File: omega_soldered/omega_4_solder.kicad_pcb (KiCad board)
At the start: 2 copper layers, 204.8 x 76.2 mm, 77 parts, among them U1 ProMicro

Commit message: generate production files
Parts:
- removed H1, H2, H3, H4: Hole, MountingHole:MountingHole_2.2mm_M2
- added MX37: MX-NoLED, MX_Only:MXOnly-6U-Centered-ReversedStabilizers-NoLED, F.Cu at (167.8, 122.7)
- moved D33 10.7 mm to (176.1, 124.9)
- moved JP1 4.83 mm to (56.7, 55.4)
- moved D1 0.88 mm to (66.2, 65.7)
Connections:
- U1 pad 10: COL7 -> ROW2
- U1 pad 11: COL6 -> ROW3
- U1 pad 12: COL5 -> COL2
- U1 pad 13: COL4 -> COL5
- U1 pad 14: COL3 -> COL6
- U1 pad 15: COL2 -> COL7
- U1 pad 16: COL1 -> COL8
- U1 pad 17: ROW0 -> COL9
- U1 pad 18: ROW1 -> COL4
- U1 pad 19: ROW2 -> COL3
- U1 pad 20: COL0 -> COL1
- U1 pad 7: Net-(U1-Pad7) -> COL0
- U1 pad 8: COL9 -> ROW0
- U1 pad 9: COL8 -> ROW1
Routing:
- net COL9: track 75.0 -> 236.2 mm
- net COL8: track 74.0 -> 213.3 mm
- net COL7: track 49.4 -> 166.9 mm
- net COL6: track 49.8 -> 145.8 mm
- net COL5: track 90.7 -> 170.4 mm
- net COL4: track 49.2 -> 116.9 mm
- net ROW3: track 175.3 -> 237.4 mm
- net COL3: track 48.9 -> 99.4 mm
- net ROW2: track 171.4 -> 212.0 mm
- net COL1: track 49.5 -> 87.9 mm
- net COL0: track 49.7 -> 84.0 mm
- net COL2: track 49.6 -> 72.9 mm
- net Net-(D33-Pad2): track 21.6 -> 42.1 mm
- net ROW1: track 171.4 -> 190.7 mm
- net ROW0: track 171.3 -> 179.8 mm
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- added copper zone on B.Cu, net GND
- added copper zone on F.Cu, net GND
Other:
- board size 204.8 x 76.2 mm -> 204.8 x 78 mm
- board text added: "6u-centered"
- board text added: "8u 10u 6u-offcenter"
- board text added: "omega4_v0 by makenova"

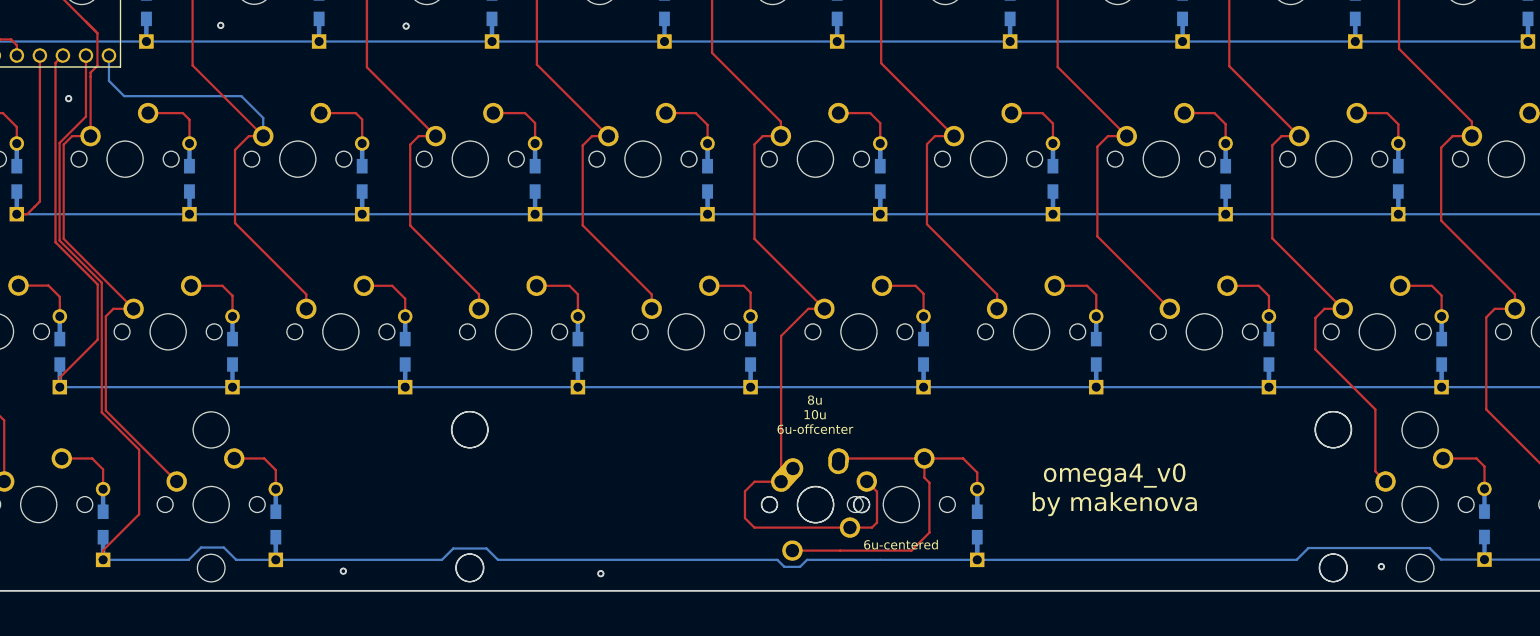
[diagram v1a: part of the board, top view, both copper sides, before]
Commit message: update spacebars on omega4
fix spacebar positioning on omega4
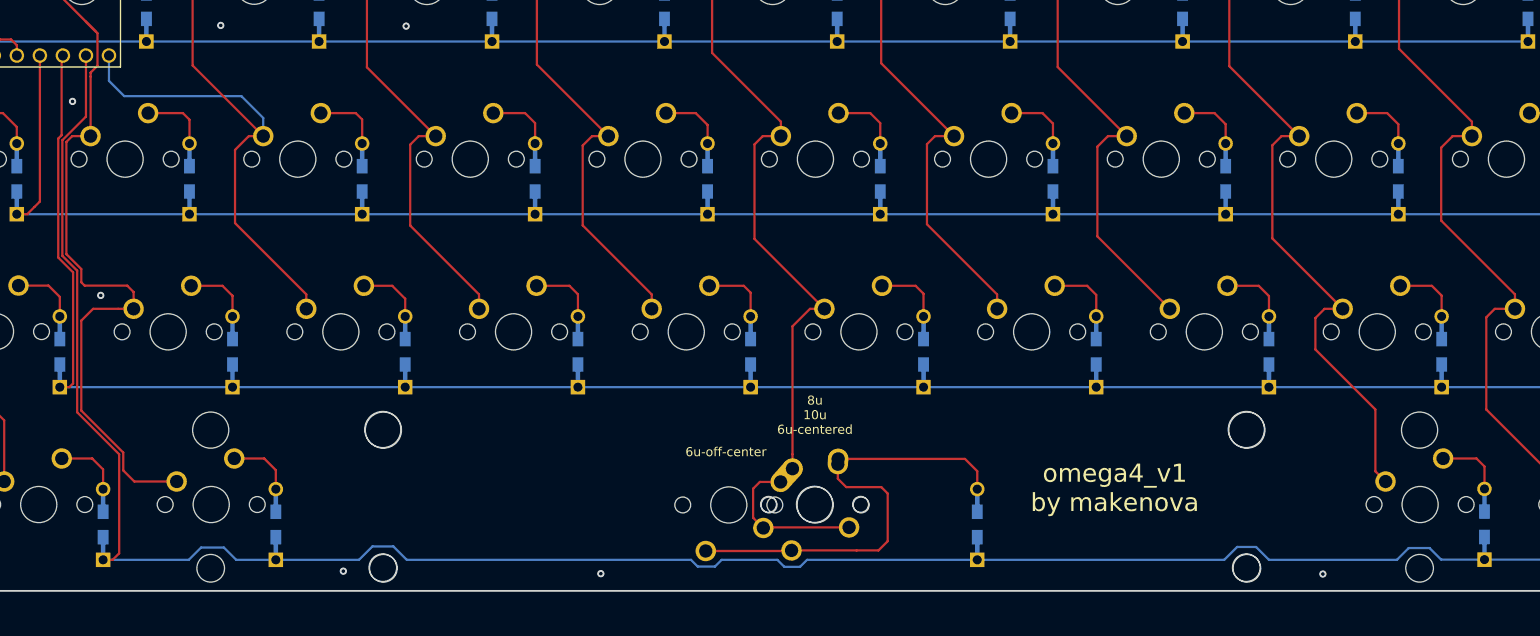
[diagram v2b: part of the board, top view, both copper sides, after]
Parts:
- MX37: footprint MX_Only:MXOnly-6U-Centered-ReversedStabilizers-NoLED -> MX_Only:MXOnly-6U-Centered-NoLED
- moved MX37 9.57 mm to (158.2, 122.7), turned to 180 degrees
- moved MX36 9.56 mm to (158.2, 122.7)
- moved MX33 0.06 mm to (158.2, 122.7)
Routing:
- net COL5: track 170.4 -> 158.3 mm
- net Net-(D33-Pad2): track 42.1 -> 51.4 mm
- net COL1: track 87.9 -> 96.7 mm
- net ROW2: track 212.0 -> 210.1 mm
- net ROW3: track 237.4 -> 237.9 mm
- net GND: vias 10 -> 11
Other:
- board text added: "6u-off-center"
- board text added: "8u 10u 6u-centered"
- board text added: "omega4_v1 by makenova"
- board text removed: "6u-centered"
- board text removed: "8u 10u 6u-offcenter"
- board text removed: "omega4_v0 by makenova"

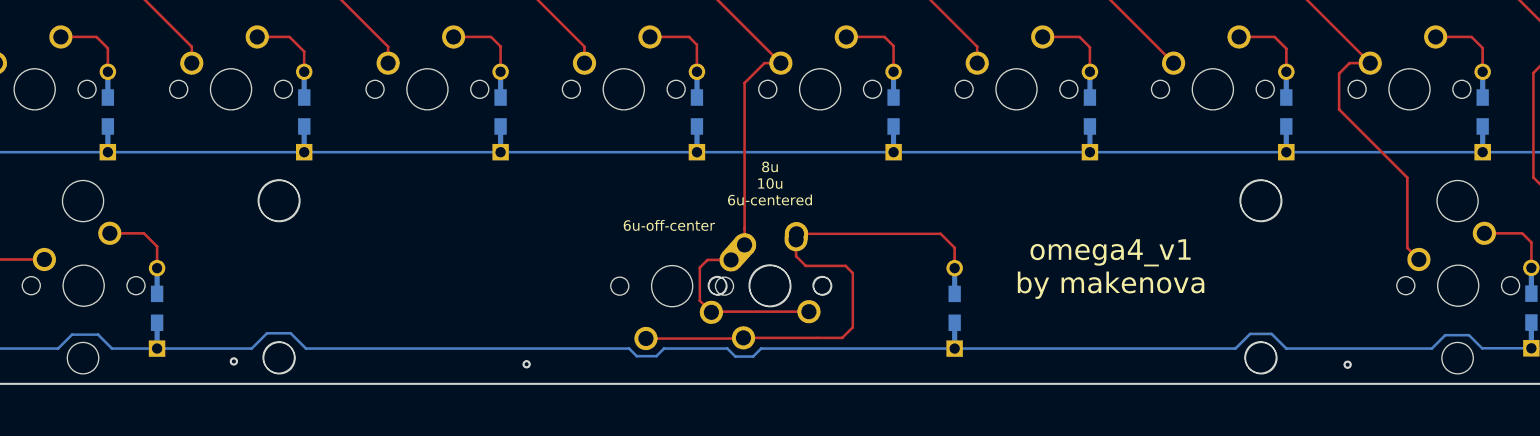
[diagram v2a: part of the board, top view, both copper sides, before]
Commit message: update omega4 case files
move stabilizer cutouts
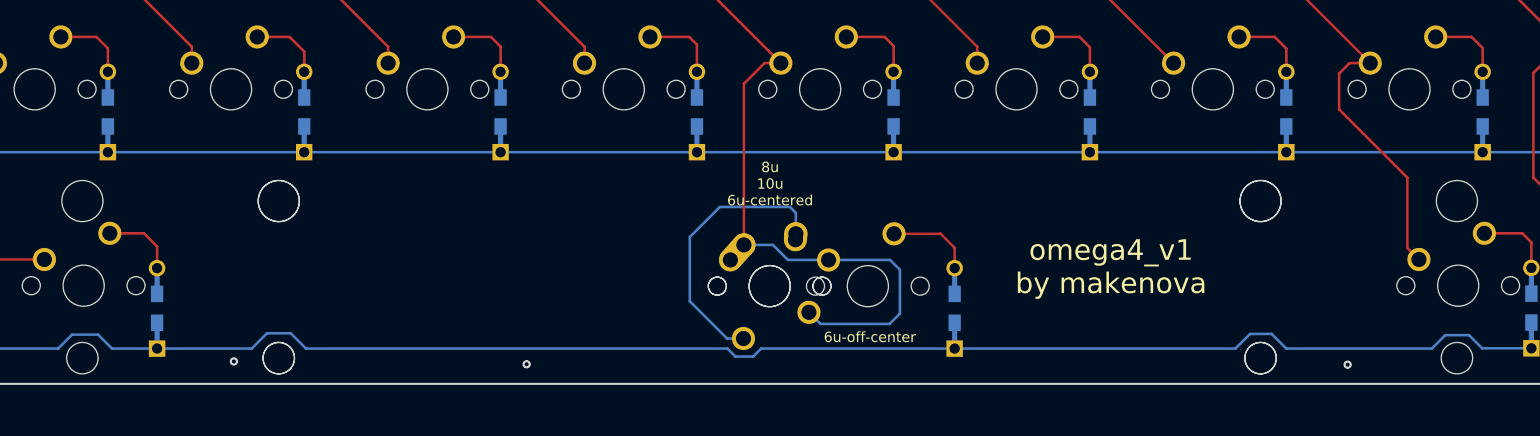
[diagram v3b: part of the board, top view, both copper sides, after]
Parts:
- MX36: footprint MX_Only:MXOnly-6U-NoLED -> MX_Only:MXOnly-6U-ReversedStabilizers-NoLED
- moved MX37 0.06 mm to (158.2, 122.7)
- moved MX33 0.06 mm to (158.2, 122.7)
- moved MX36 0.06 mm to (158.2, 122.7), turned to 0 degrees
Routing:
- net Net-(D33-Pad2): track 51.4 -> 35.2 mm
- net COL5: track 158.3 -> 170.8 mm
- net ROW3: track 237.9 -> 237.3 mm

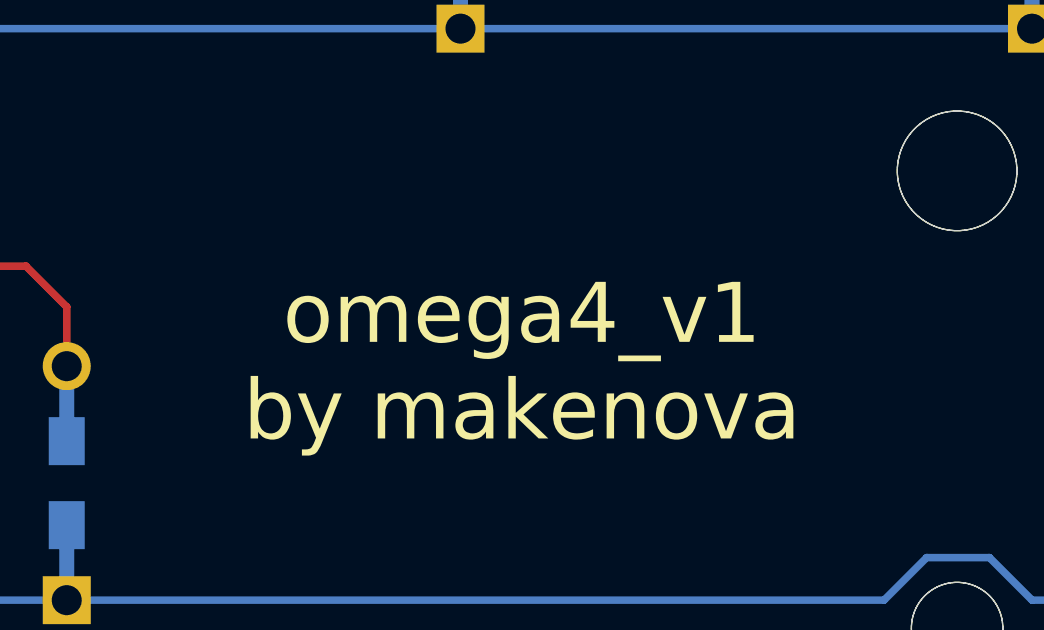
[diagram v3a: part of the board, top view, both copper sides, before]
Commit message: update soldered omega
increase stanoff hole size through the pcb
update stl files and step files
shuffle file locations
regenerate gerbers
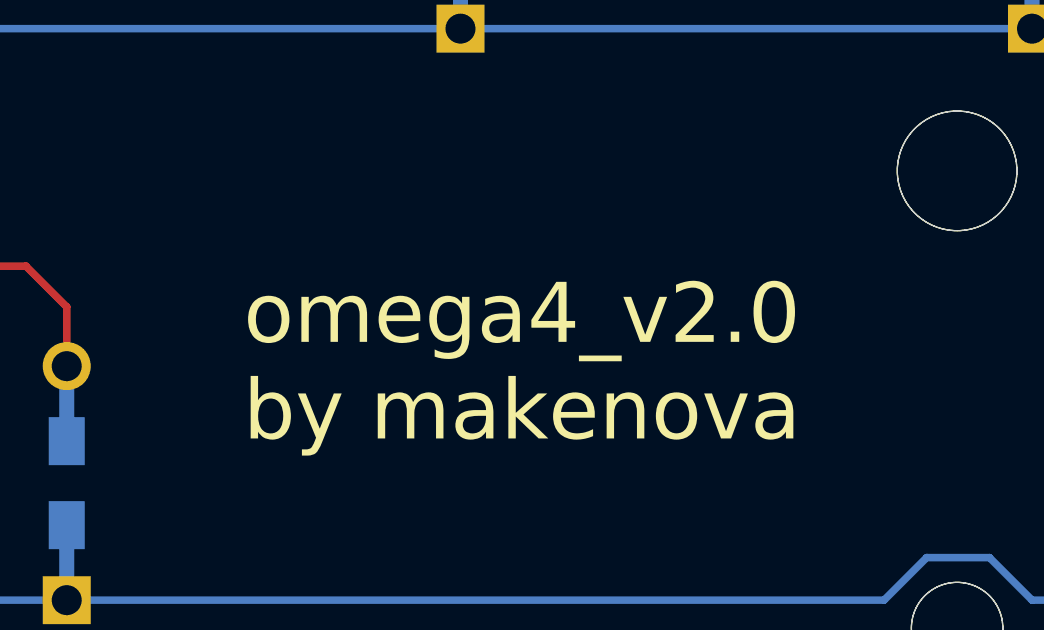
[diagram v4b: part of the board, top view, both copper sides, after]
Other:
- board text added: "omega4_v2.0 by makenova"
- board text removed: "omega4_v1 by makenova"
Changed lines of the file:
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@@
     (effects (font (size 1 1) (thickness 0.15)))
   )
-  (gr_text "omega4_v1\nby makenova" (at 191.3 120.875) (layer F.SilkS)
+  (gr_text "omega4_v2.0\nby makenova" (at 191.3 120.875) (layer F.SilkS)
     (effects (font (size 2 2) (thickness 0.2)))
   )

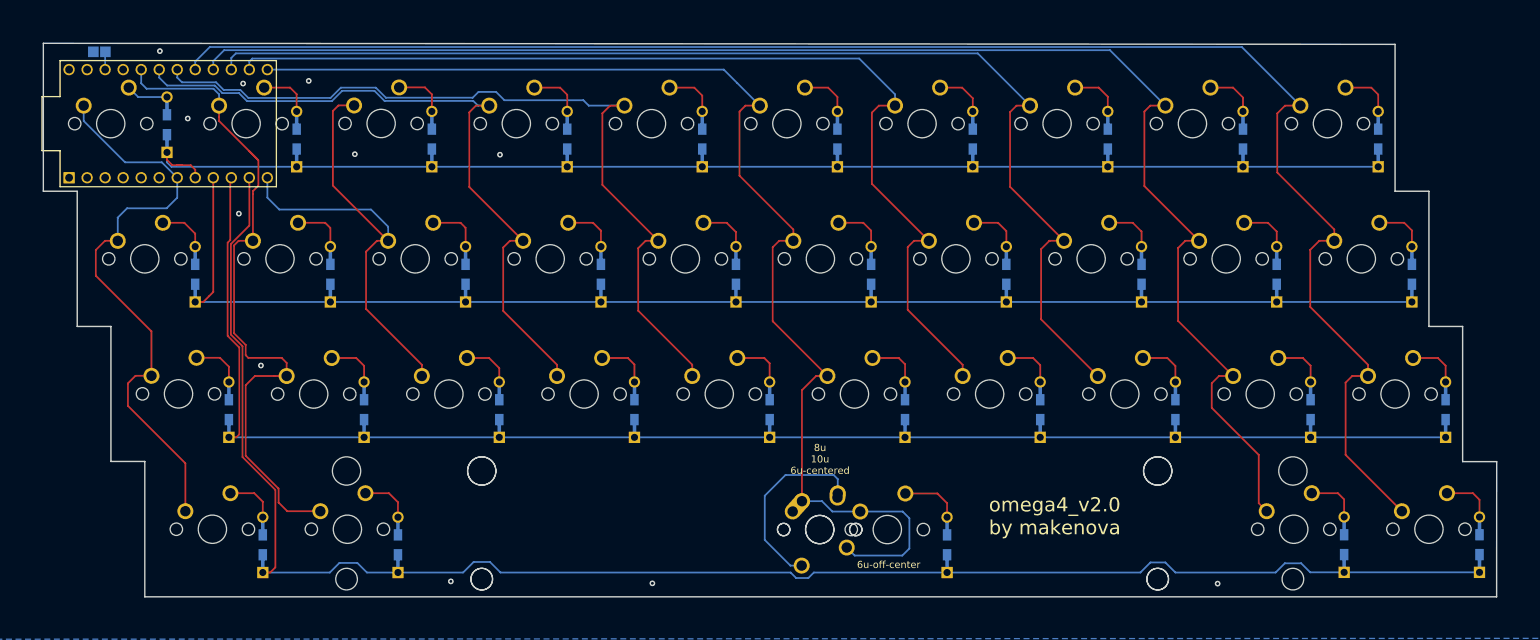
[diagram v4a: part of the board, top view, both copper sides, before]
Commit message: wip: v3
break away bottom row
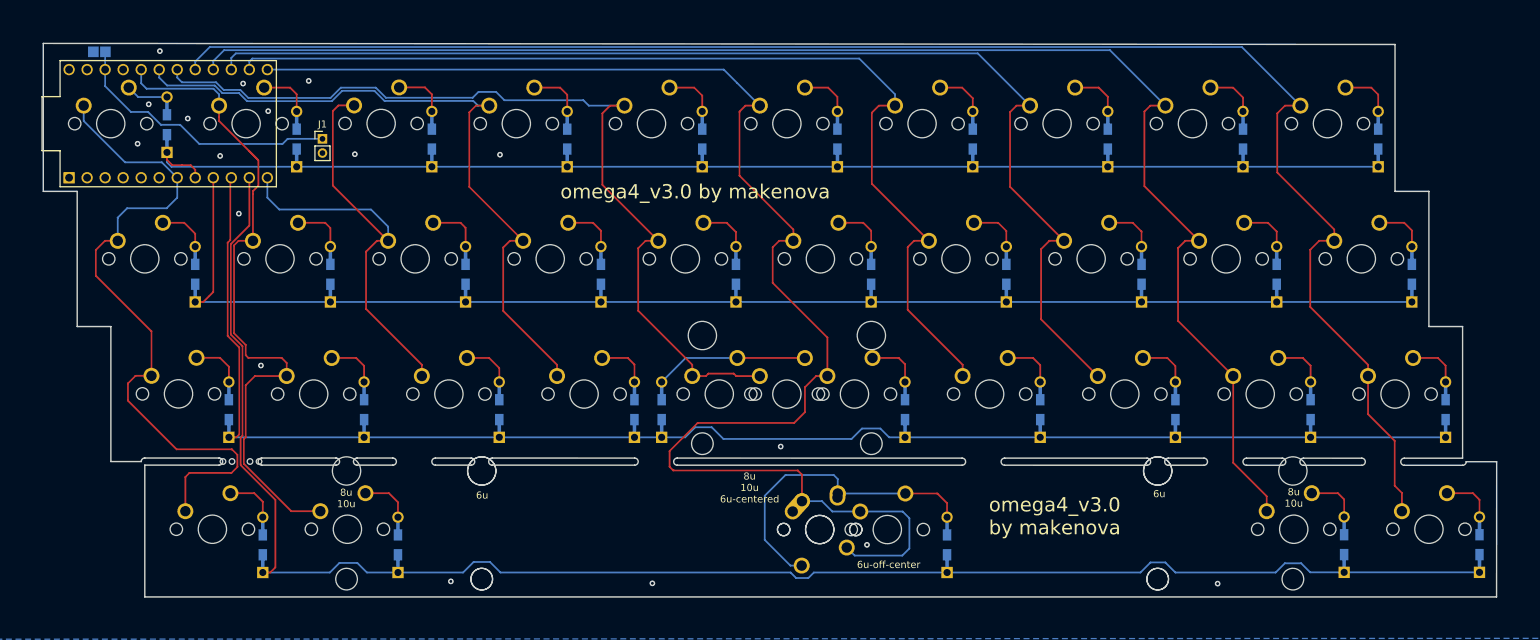
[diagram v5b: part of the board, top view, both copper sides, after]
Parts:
- added G***: LOGO, LOGO, B.Cu at (154.0, 81.3)
- added J1: Conn_01x02_Female, Connector_PinHeader_2.00mm:PinHeader_1x02_P2.00mm_Vertical, F.Cu at (88.1, 67.7)
- added MX38: MX-NoLED, MX_Only:MXOnly-2U-ReversedStabilizers-NoLED, F.Cu at (153.6, 103.7)
- added REF**: breakaway-mousebites, Keebio-Parts:breakaway-mousebites, F.Cu at (76.6, 113.4)
- moved D25 15.2 mm to (135.9, 105.8)
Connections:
- net Net-(JP1-Pad1) renamed RST
- U1 pad 1: Net-(U1-Pad1) -> unconnected-(U1-Pad1)
- U1 pad 2: Net-(U1-Pad2) -> unconnected-(U1-Pad2)
- U1 pad 24: Net-(U1-Pad24) -> unconnected-(U1-Pad24)
- U1 pad 5: Net-(U1-Pad5) -> unconnected-(U1-Pad5)
- U1 pad 6: Net-(U1-Pad6) -> unconnected-(U1-Pad6)
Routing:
- net RST: track 2.52 -> 39.2 mm
- net COL5: track 170.8 -> 204.5 mm
- net COL0: track 84.0 -> 98.1 mm
- net Net-(D25-Pad2): track 7.50 -> 21.6 mm
- net COL4: track 116.9 -> 126.7 mm
- net Net-(D33-Pad2): track 35.2 -> 44.9 mm
- net COL9: track 236.2 -> 232.2 mm
- net COL8: track 213.3 -> 209.6 mm
- net ROW2: track 210.1 -> 212.5 mm
- net ROW0: track 179.8 -> 179.1 mm
- net GND: vias 11 -> 17
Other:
- outline, holes or cut-outs redrawn
- net class Default removed
- board text added: "6u"
- board text added: "8u 10u"
- board text added: "omega4_v3.0 by makenova"
- board text removed: "omega4_v2.0 by makenova"

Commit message: update mouse bites
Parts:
- added REF**: breakaway-mousebites, Keebio-Parts:breakaway-mousebites, F.Cu at (101.1, 113.4)
- added REF**: breakaway-mousebites, Keebio-Parts:breakaway-mousebites, F.Cu at (181.2, 113.4)
- added REF**: breakaway-mousebites, Keebio-Parts:breakaway-mousebites, F.Cu at (237.7, 113.4)
- added REF**: breakaway-mousebites, Keebio-Parts:breakaway-mousebites, F.Cu at (135.2, 113.4)
- added REF**: breakaway-mousebites, Keebio-Parts:breakaway-mousebites, F.Cu at (215.6, 113.4)
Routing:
- net COL5: track 204.5 -> 208.4 mm
- net COL8: track 209.6 -> 211.3 mm
- net GND: vias 17 -> 18
